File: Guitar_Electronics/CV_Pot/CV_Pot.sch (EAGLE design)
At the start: 8 parts

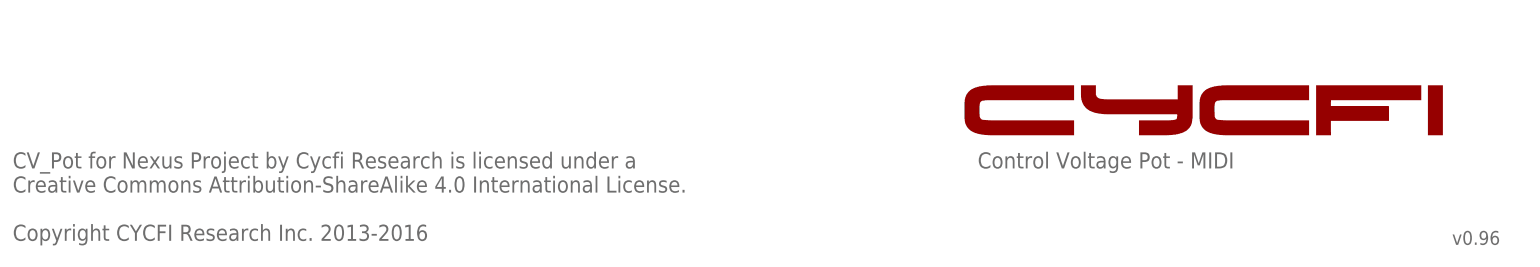
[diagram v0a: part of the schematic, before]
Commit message: Updated copyright and document number of schematics
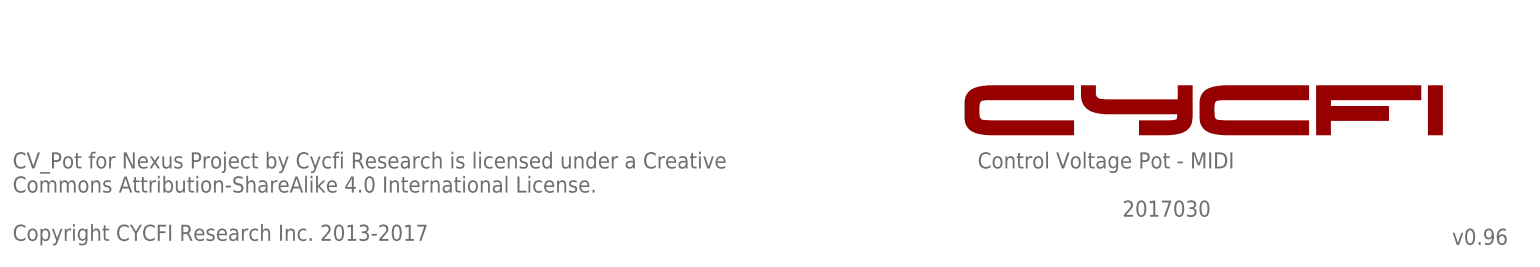
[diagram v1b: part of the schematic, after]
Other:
- note added: "2017030"
- note added: "CV_Pot for Nexus Project by Cycfi Research is licensed under a Creative Commons Attribution-ShareAlike 4.0 International License. Copyright CYCFI Research Inc. 2013-2017"
- note removed: "CV_Pot for Nexus Project by Cycfi Research is licensed under a Creative Commons Attribution-ShareAlike 4.0 International License. Copyright CYCFI Research Inc. 2013-2016"
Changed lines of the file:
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@@
 <?xml version="1.0" encoding="utf-8"?>
 <!DOCTYPE eagle SYSTEM "eagle.dtd">
-<eagle version="6.3">
+<eagle version="7.6.0">
 <drawing>
 <settings>
@@
 <text x="149.225" y="120.65" size="1.778" layer="95">GND</text>
 <text x="149.225" y="118.11" size="1.778" layer="95">OUT</text>
-<text x="237.49" y="6.985" size="2.1844" layer="95">v0.96</text>
-<text x="10.16" y="7.62" size="2.54" layer="95">CV_Pot for Nexus Project by Cycfi Research is licensed under a
-Creative Commons Attribution-ShareAlike 4.0 International License.
-Copyright CYCFI Research Inc. 2013-2016</text>
+<text x="237.49" y="6.985" size="2.54" layer="95">v0.96</text>
+<text x="10.16" y="7.62" size="2.54" layer="95">CV_Pot for Nexus Project by Cycfi Research is licensed under a Creative
+Commons Attribution-ShareAlike 4.0 International License.
+Copyright CYCFI Research Inc. 2013-2017</text>
 <rectangle x1="164.56469375" y1="24.29065625" x2="177.7930125" y2="24.29954375" layer="94"/>
 <rectangle x1="188.043184375" y1="24.29065625" x2="192.443734375" y2="24.29954375" layer="94"/>
@@
 <rectangle x1="216.011125" y1="32.176084375" x2="232.62653125" y2="32.184971875" layer="94"/>
 <rectangle x1="233.675553125" y1="32.176084375" x2="236.031403125" y2="32.184971875" layer="94"/>
+<text x="185.42" y="11.43" size="2.54" layer="95">2017030</text>
 </plain>
 <instances>

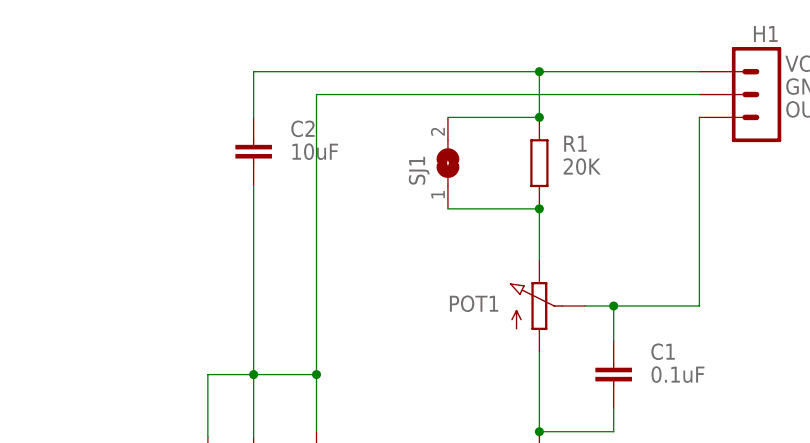
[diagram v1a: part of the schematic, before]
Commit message: Change 10uF to 1uF in the schematics and BOM file
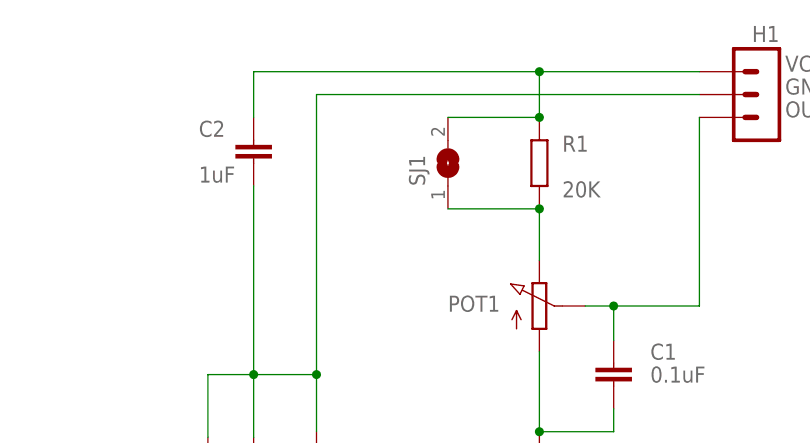
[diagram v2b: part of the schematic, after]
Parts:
- C2: value 10uF -> 1uF
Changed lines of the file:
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@@
 <?xml version="1.0" encoding="utf-8"?>
 <!DOCTYPE eagle SYSTEM "eagle.dtd">
-<eagle version="7.6.0">
+<eagle version="6.3">
 <drawing>
 <settings>
@@
 <part name="R1" library="resistor" deviceset="R-EU_" device="R0402" value="20K"/>
 <part name="SJ1" library="jumper" deviceset="SJ" device=""/>
-<part name="C2" library="resistor" deviceset="C-EU" device="C0805" value="10uF"/>
+<part name="C2" library="resistor" deviceset="C-EU" device="C0805" value="1uF"/>
 </parts>
 <sheets>
@@
 <instance part="R1" gate="G$1" x="121.92" y="113.03" smashed="yes" rot="R90">
 <attribute name="NAME" x="124.46" y="114.3" size="1.778" layer="95"/>
-<attribute name="VALUE" x="124.46" y="111.76" size="1.778" layer="96"/>
+<attribute name="VALUE" x="124.46" y="109.22" size="1.778" layer="96"/>
 </instance>
 <instance part="SJ1" gate="1" x="111.76" y="113.03" rot="R90"/>
 <instance part="C2" gate="G$1" x="90.17" y="115.57" smashed="yes">
-<attribute name="NAME" x="94.234" y="115.951" size="1.778" layer="95"/>
-<attribute name="VALUE" x="94.234" y="113.411" size="1.778" layer="96"/>
+<attribute name="NAME" x="84.074" y="115.951" size="1.778" layer="95"/>
+<attribute name="VALUE" x="84.074" y="110.871" size="1.778" layer="96"/>
 </instance>
 </instances>
